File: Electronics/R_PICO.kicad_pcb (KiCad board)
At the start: 2 copper layers, 17 parts, among them J1 Battery_Connector, J10 MotorR, J2 VL53L0X, J3 VL53L0X, J4 VL53L0X, J5 VL53L0X, J6 KTIR0711S, J7 KTIR0711S, J8 TB6612FNG, J9 MotorL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

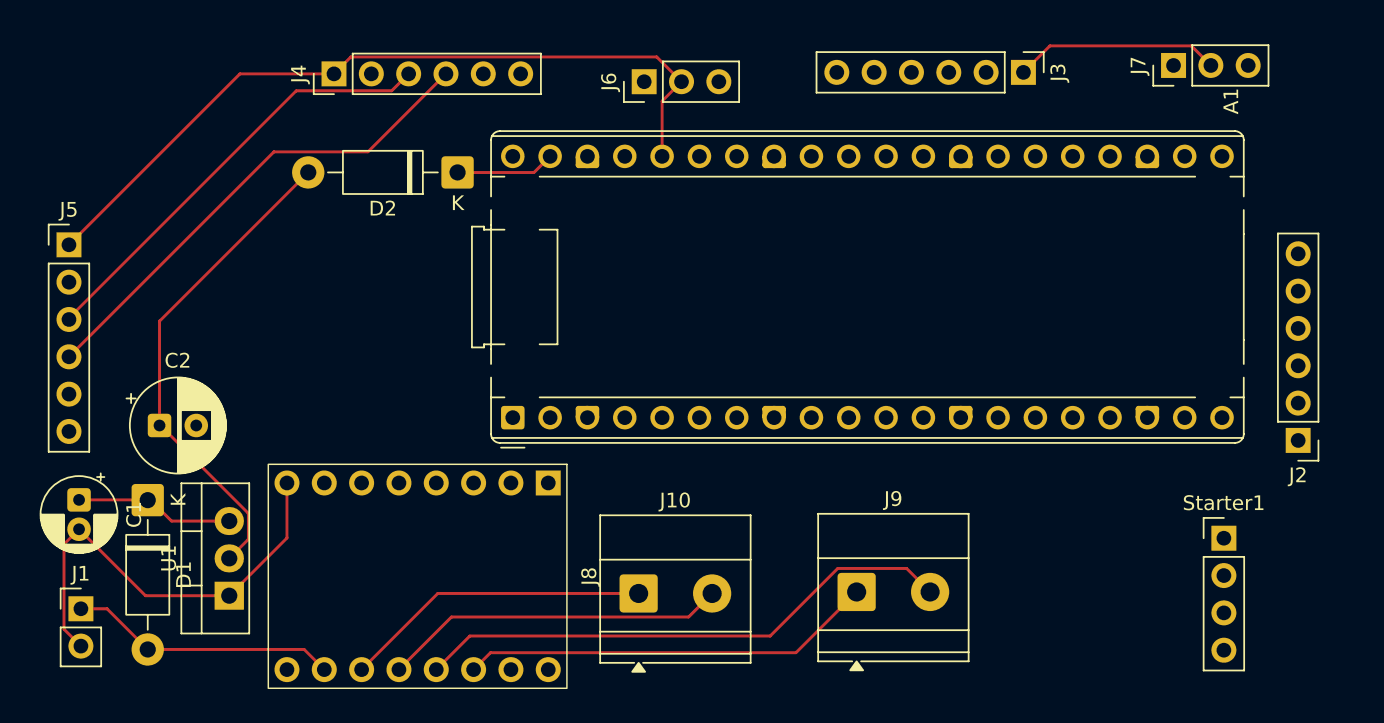
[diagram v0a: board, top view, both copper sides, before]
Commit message: Feat: Finished PCB schematic, awaiting fabrication decision
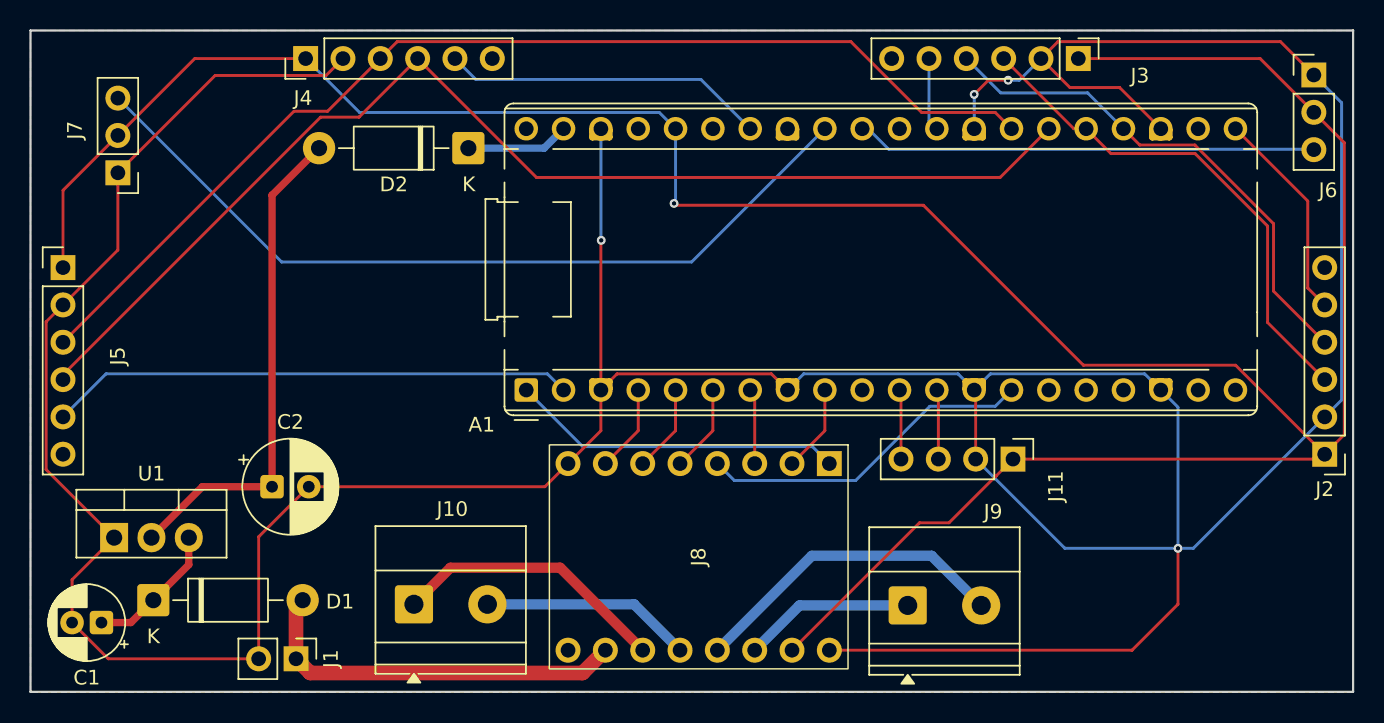
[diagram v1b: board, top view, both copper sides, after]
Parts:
- removed Starter1: ~, Connector_PinHeader_2.54mm:PinHeader_1x04_P2.54mm_Vertical
- added J11: Starter, Connector_PinHeader_2.54mm:PinHeader_1x04_P2.54mm_Vertical, F.Cu at (236.9, 69.2)
- moved J7 72.2 mm to (175.9, 49.7), turned to 180 degrees
- moved J6 45.6 mm to (257.3, 43.0), turned to 0 degrees
- moved J8 19.2 mm to (215.5, 75.8)
- moved J10 15.3 mm to (196.1, 79.0)
- moved J1 15.0 mm to (188.1, 82.8), turned to -90 degrees
- moved U1 8.77 mm to (175.7, 74.5), turned to 0 degrees
- moved C2 8.72 mm to (186.4, 71.0)
- moved C1 8.49 mm to (174.8, 80.3), turned to 180 degrees
- moved D1 6.82 mm to (178.4, 78.8), turned to 0 degrees
- moved J3 3.85 mm to (241.3, 41.9)
- moved J9 3.59 mm to (229.7, 79.1)
- moved J4 2.19 mm to (188.7, 41.9)
- moved A1 2.09 mm to (203.7, 64.5)
- moved J2 2.03 mm to (258.1, 68.8)
- moved D2 1.81 mm to (199.8, 48.0)
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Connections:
- A1 pad 10: /scl1 -> unconnected-(A1-GPIO7-Pad10)
- A1 pad 15: /A1 -> unconnected-(A1-GPIO11-Pad15)
- A1 pad 16: /A2 -> unconnected-(A1-GPIO12-Pad16)
- A1 pad 17: /B1 -> unconnected-(A1-GPIO13-Pad17)
- A1 pad 19: /B2 -> unconnected-(A1-GPIO14-Pad19)
- A1 pad 2: unconnected-(A1-GPIO1-Pad2) -> /XSHUT_LEFT
- A1 pad 21: unconnected-(A1-GPIO16-Pad21) -> /XSHUT_RIGHT
- A1 pad 24: Net-(A1-GPIO18) -> /SDA1
- A1 pad 25: Net-(A1-GPIO19) -> /SCL1
- A1 pad 29: unconnected-(A1-GPIO22-Pad29) -> /XSHUT_FRONT_RIGHT
- A1 pad 34: unconnected-(A1-GPIO28_ADC2-Pad34) -> /XSHUT_FRONT_LEFT
- A1 pad 5: unconnected-(A1-GPIO3-Pad5) -> /B2
- A1 pad 6: Net-(A1-GPIO4) -> /B1
- A1 pad 7: Net-(A1-GPIO5) -> /A1
- A1 pad 9: /sda1 -> /A2
- J2 pad 3: /scl1 -> /SCL1
- J2 pad 4: /sda1 -> /SDA1
- J2 pad 5: Net-(A1-GPIO5) -> /XSHUT_RIGHT
- J3 pad 3: /scl1 -> /SCL1
- J3 pad 4: /sda1 -> /SDA1
- J3 pad 5: Net-(A1-GPIO4) -> /XSHUT_FRONT_RIGHT
- J4 pad 5: Net-(A1-GPIO18) -> /XSHUT_FRONT_LEFT
- J5 pad 5: Net-(A1-GPIO19) -> /XSHUT_LEFT
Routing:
- net GND: track 30.2 -> 301.3 mm, vias 0 -> 4
- net /3V3: track 67.4 -> 193.1 mm, vias 0 -> 1
- net /ADC1: track 0.00 -> 56.5 mm
- net /sda0: track 33.6 -> 81.0 mm
- net /scl0: track 30.1 -> 75.5 mm
- net /XSHUT_LEFT: track 0.00 -> 35.7 mm
- net /SDA1: track 0.00 -> 35.1 mm
- net /SCL1: track 0.00 -> 34.7 mm
- net /ADC0: track 0.00 -> 31.3 mm
- net /GP10: track 0.00 -> 23.0 mm
- net /PWM0A: track 0.00 -> 22.7 mm
- net /XSHUT_FRONT_LEFT: track 0.00 -> 22.1 mm
- net /MOT1_IN: track 28.3 -> 11.7 mm
- net /MOT1_OUT: track 37.1 -> 22.0 mm
- net /XSHUT_RIGHT: track 0.00 -> 14.5 mm
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- added copper zone on B.Cu, net GND
- added copper zone on F.Cu, net GND
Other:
- board outline added: 90 x 45 mm
